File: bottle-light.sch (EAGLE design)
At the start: 57 parts, among them IC1 STM32F334K8T, IC2 LF33, X1 78127-1128, X2 UJ2-MIBH-4-SMT-TR, X3 SWD

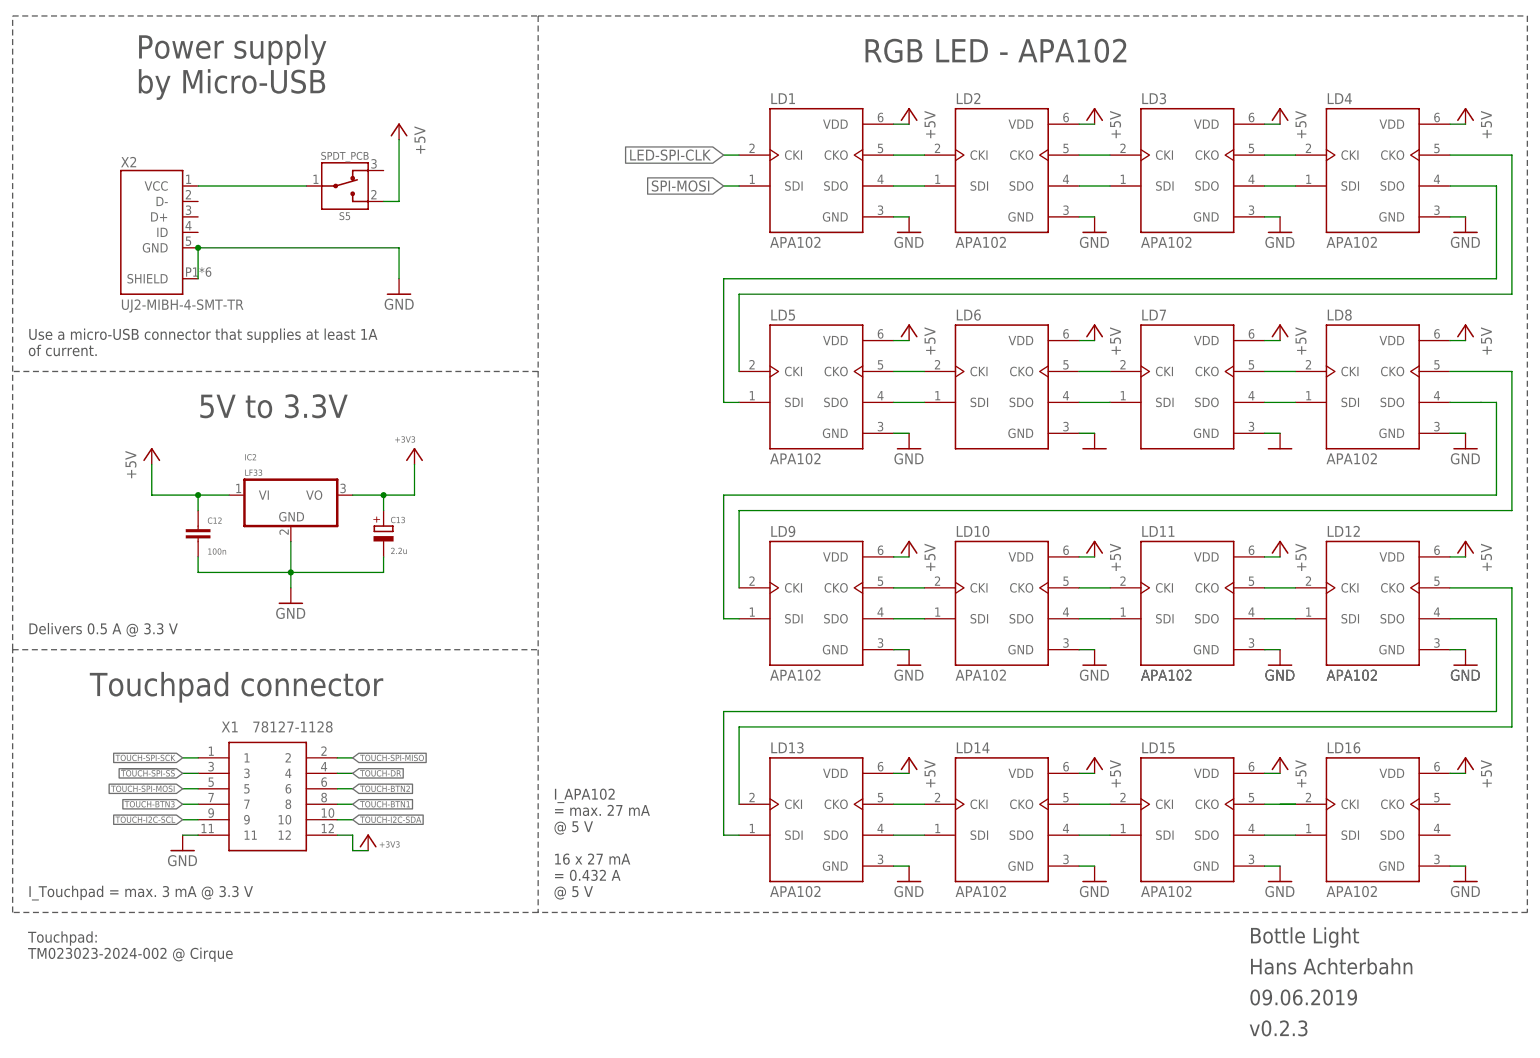
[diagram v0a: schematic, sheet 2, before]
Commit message: v0.2.4 Device of Micro-USB  connector was defect -> repaired | removed buttons and color potentiometer | added incremental encoder | connected touch pad connector to I2C of STM32 | added MIT license | added a connector for connecting an optional APA102 Strip
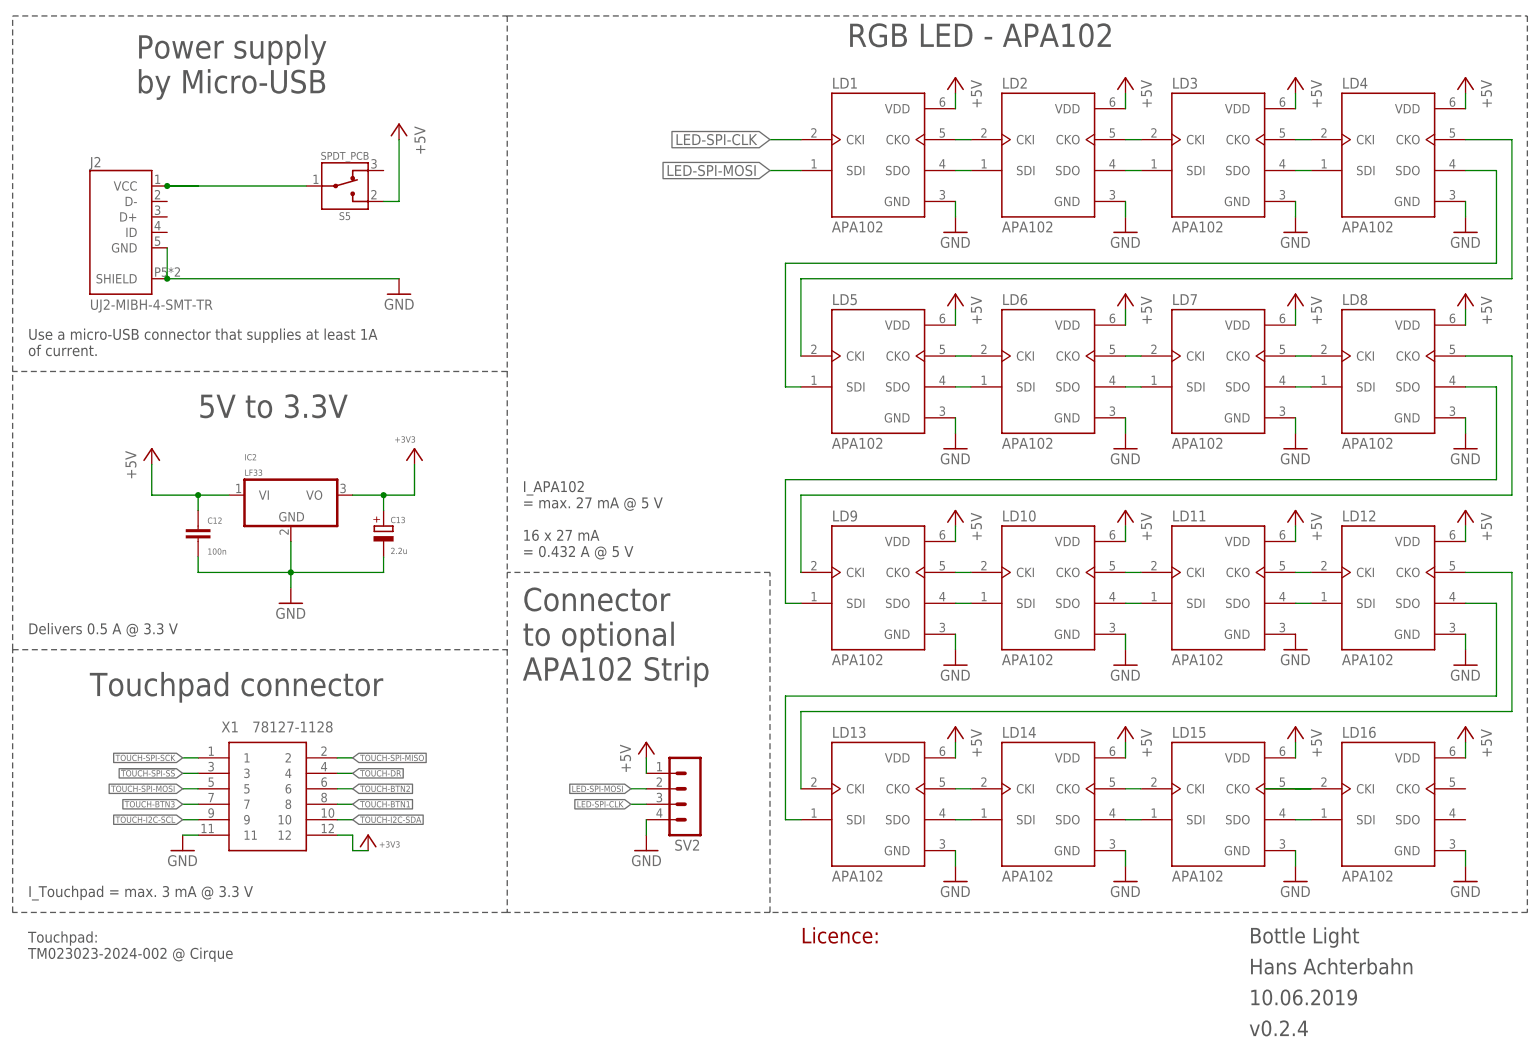
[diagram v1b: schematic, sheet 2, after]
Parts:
- removed C8, C9: 100n, resistor:C-EUC0603
- removed R25: 10k, h8-rlc:POT_RK09K
- removed R29: 8.2, resistor:R-EU_R0603
- removed R33, R36: 100R, rcl:R-EU_R0603
- removed R34, R37: 100k, rcl:R-EU_R0603
- removed R35, R38: 330R, rcl:R-EU_R0603
- removed S2, S3, S4: ALPS-SKHH, h8-switch:ALPS-SKHH-SHIELD
- removed X2: UJ2-MIBH-4-SMT-TR, UJ2-MIBH-4-SMT-TR:UJ2-MIBH-4-SMT-TR
- added J2: UJ2-MIBH-4-SMT-TR, UJ2-MIBH-4-SMT-TR:UJ2-MIBH-4-SMT-TRCUIINC_UJ2-MIBH-4-SMT-TR-2
- added R6, R7: 3k3, rcl:R-EU_R0603
- added SV2: (no value), con-lstb:MA04-1
- added U1: EC11B15242AZ, EC11B15242AZ:EC11B15242AZ
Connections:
- net USER-BUTTON1 renamed ENCODER-BUTTON
- removed net N$29: IC1G$1.PA0, R29.2
- removed net N$32: R33.1, R34.2, R35.2, S3.1
- removed net N$33: C8.2, R33.2
- removed net N$35: R36.1, R37.2, R38.2, S4.1
- removed net N$36: C9.2, R36.2
- removed net POTI-COLOR: R25.S, R29.1
- removed net SPI-MOSI: LD1.SDI
- removed net USER-BUTTON2: IC1G$2.PA9, R35.1
- removed net USER-BUTTON3: IC1G$2.PA10, R38.1
- new net ENCODER-A: IC1G$2.PA9, R7.2, U1.A
- new net ENCODER-B: IC1G$2.PA10, R6.2, U1.B
- net +3V3: now also R6.1, R7.1, U1.D; no longer C8.1, C9.1, R25.E, S2.2, S3.2, S4.2
- net +5V: now also SV2.1
- net 5V-IN: now also J2.VCC; no longer X2.VCC
- net GND: now also J2.GND, J2.SHIELD, SV2.4, U1.C, U1.MH1, U1.MH2; no longer R25.A, R25.NC1, R25.NC2, R34.1, R37.1, S2.NC1, S2.NC2, S3.NC1, S3.NC2, S4.NC1, S4.NC2, X2.GND, X2.SHIELD
- net LED-SPI-CLK: now also SV2.3
- net LED-SPI-MOSI: now also LD1.SDI, SV2.2
- net N$30: now also U1.E; no longer S2.1
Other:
- note added: "Connector to optional APA102 Strip"
- note added: "I_Encoder = max. 3 mA @ 3.3 V I_Button = max. 0.04 mA @ 3.3 V"
- note added: "Incremental encoder"
- note added: "Licence:"
- note added: "License:"
- note removed: "I_Button = max. 0.04 mA @ 3.3 V 3 x 0.04 mA = 0.12 mA @ 3.3 V"
- note removed: "Push Buttons"
- moved on the sheet: C7, LD1, LD10, LD11, LD12, LD13, LD14, LD15, LD16, LD2, LD3, LD4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

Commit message: v0.2.5 changed luminosity potentiometer | potentiometer and incremental encoder set to correct position
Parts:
- R26: device h8-rlc:POT_RK09K -> h8-rlc:RK0971110
- U1: MF (none) -> ALPS; MOUSER (none) -> 688-EC11B15242AE; MPN (none) -> EC11B15242AZ
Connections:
- removed net N$34: IC1G$1.PA1, R28.2
- new net N$6: IC1G$2.PA11, R28.2
- net GND: no longer R26.NC1, R26.NC2
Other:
- moved on the sheet: R28, R31, R32

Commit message: v0.2.6 STM32 rotated 45 degrees to optimize wire routing.
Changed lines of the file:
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@@
 <attribute name="LICENSE" value="MIT License"/>
 <attribute name="PROJECT" value="Bottle Light"/>
-<attribute name="VERSION" value="v0.2.5"/>
+<attribute name="VERSION" value="v0.2.6"/>
 </attributes>
 <variantdefs>

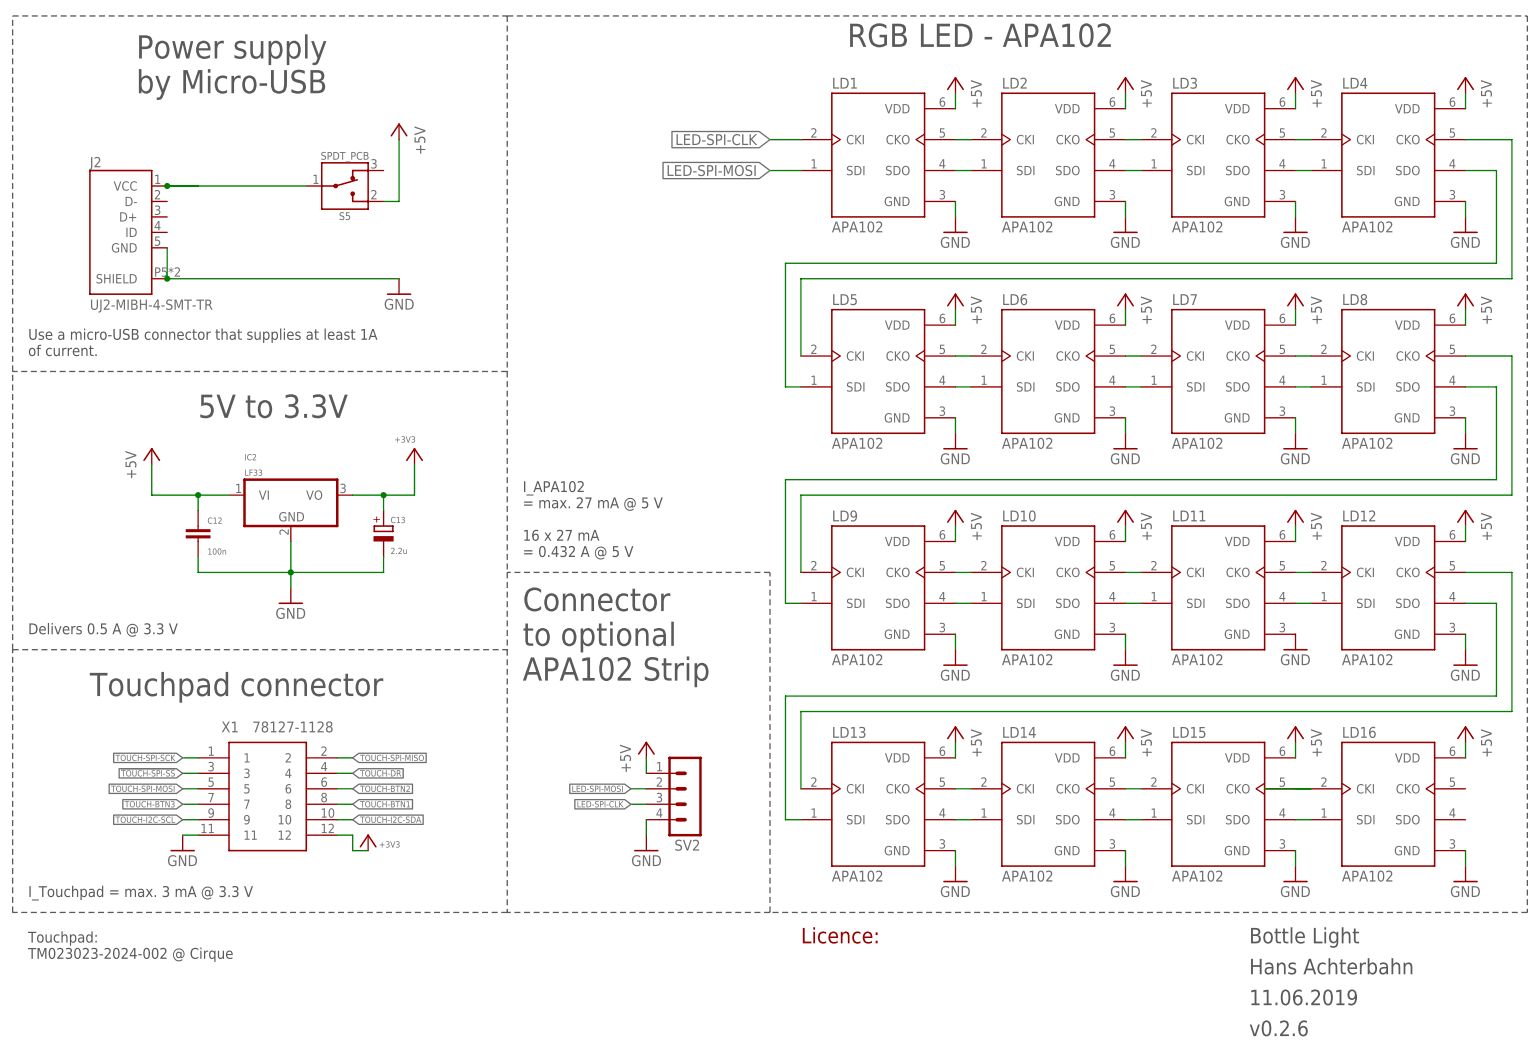
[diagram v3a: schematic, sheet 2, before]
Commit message: v0.2.7 new power switch | new restricted areas | optimized wires | checked positions of all components mounted at the edge | optimized polygon
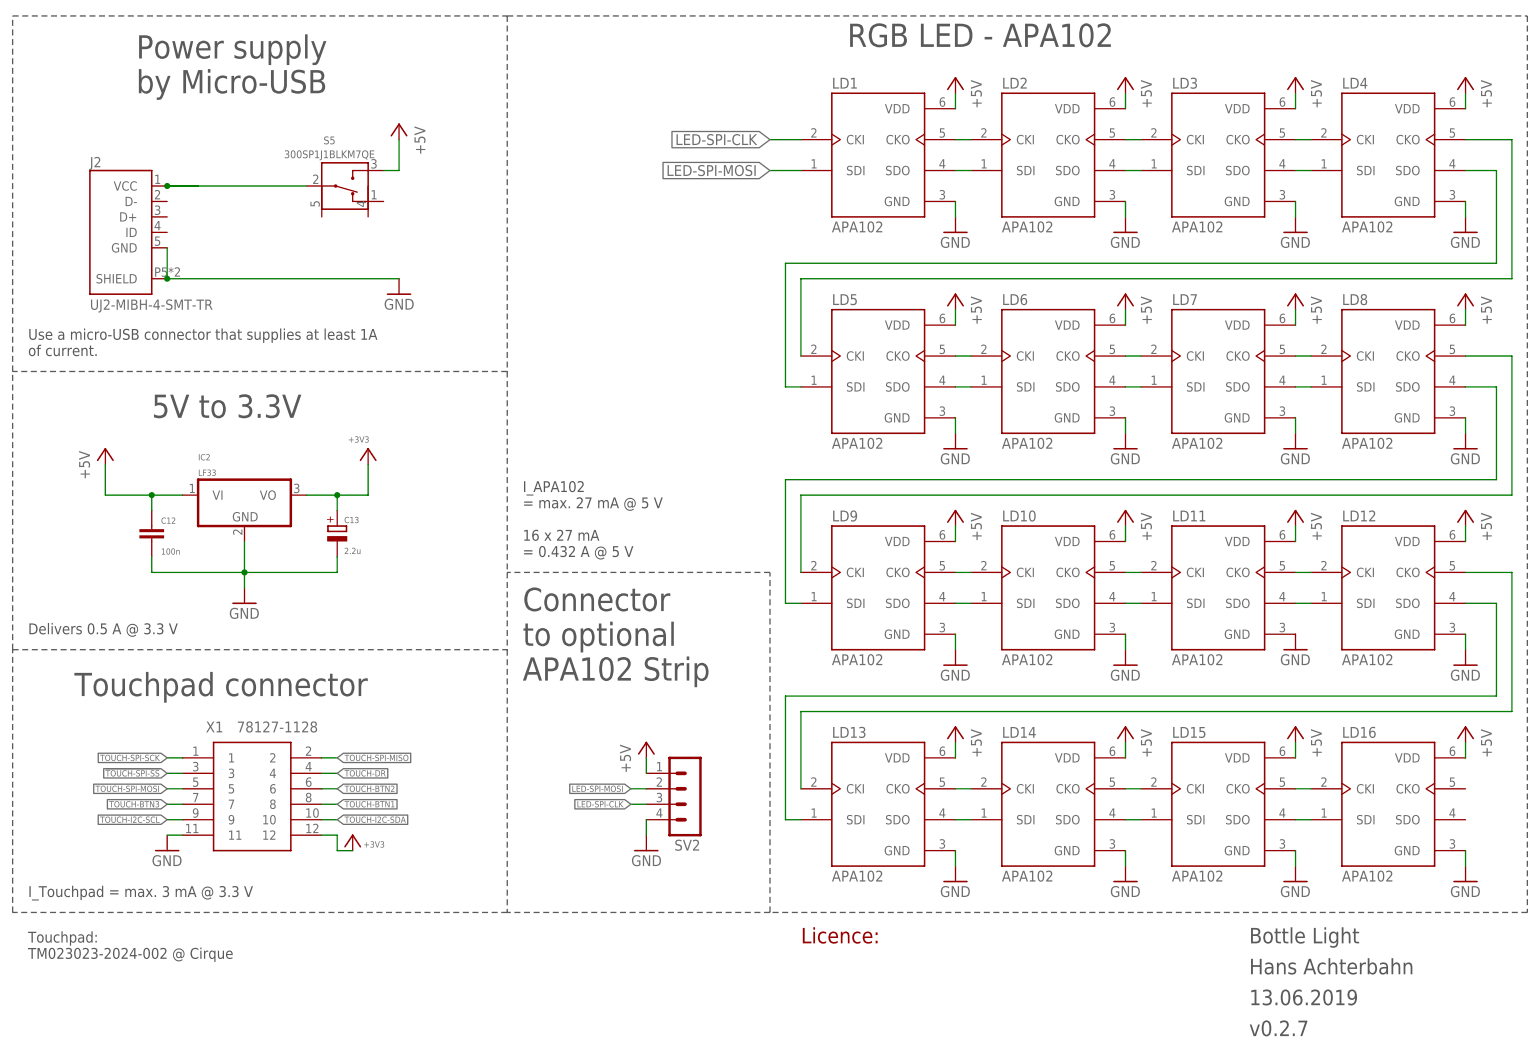
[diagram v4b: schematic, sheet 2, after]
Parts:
- added L1: BLM18, Seeed-OPL-Inductor:INDUCTOR/FERRITE-BEAD'0603'
- S5: value SPDT_PCB -> 300SP1J1BLKM7QE; device h8-switch:SPDT_PCB -> h8-switch:300SP1J1BLKM7QE
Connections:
- new net N$7: C4.1, C6.1, IC1G$5.VDDA/VREF, L1.2
- net +3V3: now also L1.1; no longer C4.1, C6.1, IC1G$5.VDDA/VREF
- net +5V: now also S5.OUT1; no longer S5.2
- net 5V-IN: now also S5.IN; no longer S5.1
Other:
- note added: "BREAD (FCM 1608KF -601T03)"
- moved on the sheet: C12, C13, C2, C3, C4, C5, C6, IC2, X1

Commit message: optimized text positions | added 2 jumpers for easy usage of additional LED strip
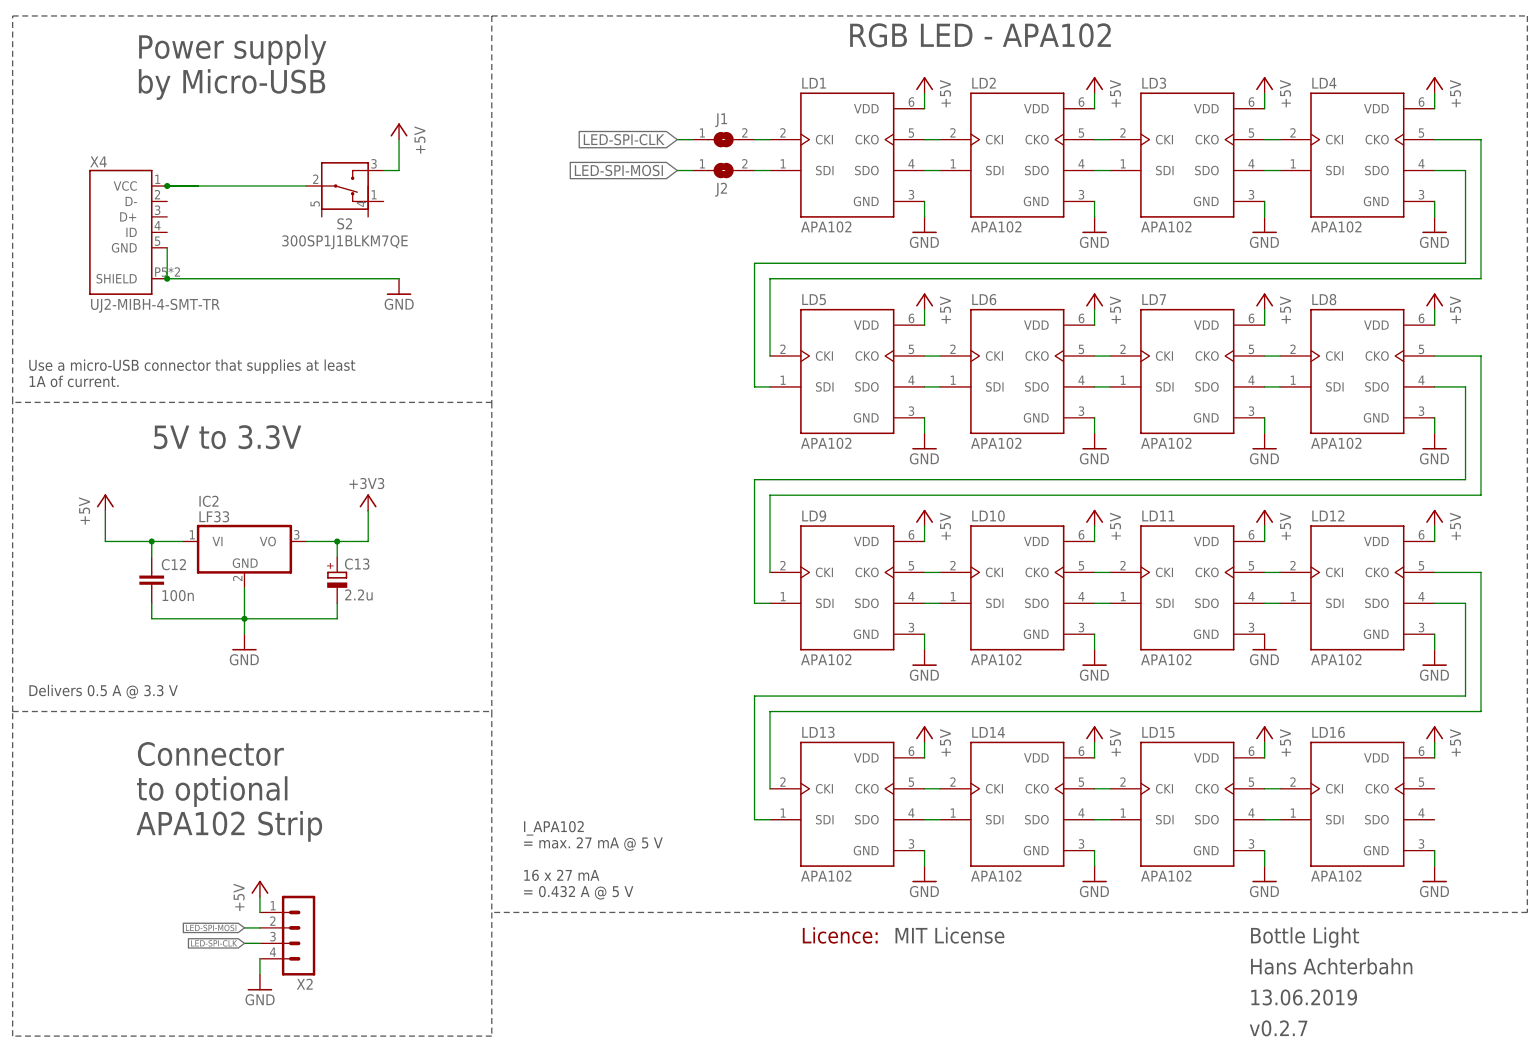
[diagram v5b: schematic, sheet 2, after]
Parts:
- removed SV2: (no value), con-lstb:MA04-1
- removed U1: EC11B15242AZ, EC11B15242AZ:EC11B15242AZ
- added J1: (no value), jumper:SJ
- added S1: EC11B15242AZ, EC11B15242AZ:EC11B15242AZ
- added X2: (no value), con-lstb:MA04-1
- added X4: UJ2-MIBH-4-SMT-TR, UJ2-MIBH-4-SMT-TR:UJ2-MIBH-4-SMT-TRCUIINC_UJ2-MIBH-4-SMT-TR-2
- J2: value UJ2-MIBH-4-SMT-TR -> (none); device UJ2-MIBH-4-SMT-TR:UJ2-MIBH-4-SMT-TRCUIINC_UJ2-MIBH-4-SMT-TR-2 -> jumper:SJ
- renumbered S5 to S2
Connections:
- new net N$8: J1.2, LD1.CKI
- new net N$9: J2.2, LD1.SDI
- net +3V3: now also S1.D; no longer U1.D
- net +5V: now also X2.1; no longer SV2.1
- net 5V-IN: now also X4.VCC; no longer J2.VCC
- net ENCODER-A: now also S1.A; no longer U1.A
- net ENCODER-B: now also S1.B; no longer U1.B
- net GND: now also S1.C, S1.MH1, S1.MH2, X2.4, X4.GND, X4.SHIELD; no longer J2.GND, J2.SHIELD, SV2.4, U1.C, U1.MH1, U1.MH2
- net LED-SPI-CLK: now also J1.1, X2.3; no longer LD1.CKI, SV2.3
- net LED-SPI-MOSI: now also J2.1, X2.2; no longer LD1.SDI, SV2.2
- net N$30: now also S1.E; no longer U1.E
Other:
- moved on the sheet: C12, C13, C7, IC2, LD1, LD10, LD11, LD12, LD13, LD14, LD15, LD16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

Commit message: Vias verkleinert | 3D Modelle hinzugefügt | auf Fusion gepusht
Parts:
- C13: device rcl:CPOL-EUUD-5X5,8 -> rcl:CPOL-EU153CLV-0505
- LD1, LD10, LD11, LD12, LD13, LD14, LD15, LD16, LD2, LD3, LD4, LD5, LD6, LD7, LD8, LD9: device 3587:APA102APA102C-5050 -> h8-optic:APA102APA102C-5050
- S1: device EC11B15242AZ:EC11B15242AZ -> h8-switch:EC11B15242AZ
- X1: device SamaSys:78127-1128 -> h8-conector:78127-1128
- X2: value (none) -> 61300411121; device con-lstb:MA04-1 -> Headers:61300411121

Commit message: changed some footprint drawings
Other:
- note added: "URL:"
- note added: "https://github.com/ HansAchterbahn/bottle-light"
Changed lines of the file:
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@@
 <schematic xreflabel="%F%N/%S.%C%R" xrefpart="/%S.%C%R">
 <attributes>
-<attribute name="DATE" value="27.06.2019"/>
+<attribute name="DATE" value="04.07.2019"/>
 <attribute name="EDITOR" value="Hans Achterbahn"/>
 <attribute name="LICENSE" value="MIT License"/>
 <attribute name="PROJECT" value="Bottle Light"/>
-<attribute name="VERSION" value="v0.2.7"/>
+<attribute name="VERSION" value="v0.2.8"/>
 </attributes>
 <variantdefs>
@@
 TM023023-2024-002 @ Cirque </text>
 <wire x1="175.26" y1="172.72" x2="175.26" y2="91.44" width="0.1524" layer="97" style="longdash"/>
+<text x="144.78" y="12.7" size="2.54" layer="97" align="top-left">https://github.com/
+HansAchterbahn/bottle-light</text>
+<text x="134.62" y="12.7" size="2.54" layer="94" align="top-left">URL:</text>
 </plain>
 <instances>
